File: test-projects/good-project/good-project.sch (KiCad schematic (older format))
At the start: 3 parts, among them J1 Conn_01x02

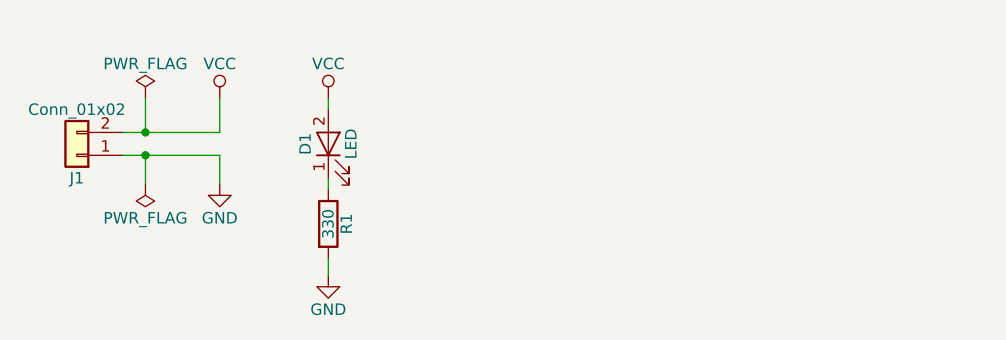
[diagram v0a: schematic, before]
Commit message: Handle schematic being created by newer versions of eeschema
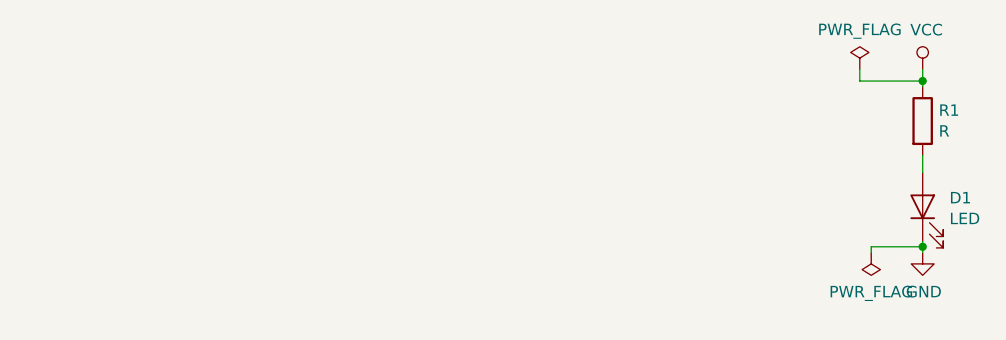
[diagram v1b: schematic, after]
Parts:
- removed D1: LED, LED_SMD:LED_0805_2012Metric, symbol LED
- removed J1: Conn_01x02, Connector_PinHeader_2.54mm:PinHeader_1x02_P2.54mm_Vertical, symbol Conn_01x02
- removed R1: 330, Resistor_SMD:R_0603_1608Metric, symbol R
- added D1: LED, symbol Device:LED
- added R1: R, symbol Device:R
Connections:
- net GND: now also D1.1 (K)
- net VCC: now also R1.1
- new net: D1.2 (A), R1.2
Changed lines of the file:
@@
-EESchema Schematic File Version 2
+EESchema Schematic File Version 4
 LIBS:good-project-cache
-EELAYER 25 0
+EELAYER 26 0
 EELAYER END
 $Descr A4 11693 8268
@@
 $EndDescr
 $Comp
-L R R1
-U 1 1 5CA32696
-P 3100 3425
-F 0 "R1" V 3180 3425 50  0000 C CNN
-F 1 "330" V 3100 3425 50  0000 C CNN
-F 2 "Resistor_SMD:R_0603_1608Metric" V 3030 3425 50  0001 C CNN
-F 3 "" H 3100 3425 50  0001 C CNN
-	1    3100 3425
+L Device:R R1
+U 1 1 5CA75BFC
+P 5700 2975
+F 0 "R1" H 5770 3021 50  0000 L CNN
+F 1 "R" H 5770 2930 50  0000 L CNN
+F 2 "" V 5630 2975 50  0001 C CNN
+F 3 "" H 5700 2975 50  0001 C CNN
+	1    5700 2975
 	1    0    0    -1
 $EndComp
 $Comp
-L LED D1
-U 1 1 5CA326B7
-P 3100 3075
-F 0 "D1" H 3100 3175 50  0000 C CNN
-F 1 "LED" H 3100 2975 50  0000 C CNN
-F 2 "LED_SMD:LED_0805_2012Metric" H 3100 3075 50  0001 C CNN
-F 3 "" H 3100 3075 50  0001 C CNN
-	1    3100 3075
+L Device:LED D1
+U 1 1 5CA75CA1
+P 5700 3350
+F 0 "D1" V 5738 3233 50  0000 R CNN
+F 1 "LED" V 5647 3233 50  0000 R CNN
+F 2 "" H 5700 3350 50  0001 C CNN
+F 3 "" H 5700 3350 50  0001 C CNN
+	1    5700 3350
 	0    -1   -1   0
 $EndComp
 $Comp
-L VCC #PWR01
-U 1 1 5CA32709
-P 3100 2875
-F 0 "#PWR01" H 3100 2725 50  0001 C CNN
-F 1 "VCC" H 3100 3025 50  0000 C CNN
-F 2 "" H 3100 2875 50  0001 C CNN
-F 3 "" H 3100 2875 50  0001 C CNN
-	1    3100 2875
+L power:VCC #PWR0101
+U 1 1 5CA75DE1
+P 5700 2750
+F 0 "#PWR0101" H 5700 2600 50  0001 C CNN
+F 1 "VCC" H 5717 2923 50  0000 C CNN
+F 2 "" H 5700 2750 50  0001 C CNN
+F 3 "" H 5700 2750 50  0001 C CNN
+	1    5700 2750
 	1    0    0    -1
 $EndComp
 $Comp
-L Conn_01x02 J1
-U 1 1 5CA32731
-P 2000 3125
-F 0 "J1" H 2000 3225 50  0000 C CNN
-F 1 "Conn_01x02" H 2000 2925 50  0000 C CNN
-F 2 "Connector_PinHeader_2.54mm:PinHeader_1x02_P2.54mm_Vertical" H 2000 3125 50  0001 C CNN
-F 3 "" H 2000 3125 50  0001 C CNN
-	1    2000 3125
-	-1   0    0    1
-$EndComp
-$Comp
-L VCC #PWR02
-U 1 1 5CA327B9
-P 2625 2875
-F 0 "#PWR02" H 2625 2725 50  0001 C CNN
-F 1 "VCC" H 2625 3025 50  0000 C CNN
-F 2 "" H 2625 2875 50  0001 C CNN
-F 3 "" H 2625 2875 50  0001 C CNN
-	1    2625 2875
+L power:GND #PWR0102
+U 1 1 5CA75E87
+P 5700 3550
+F 0 "#PWR0102" H 5700 3300 50  0001 C CNN
+F 1 "GND" H 5705 3377 50  0000 C CNN
+F 2 "" H 5700 3550 50  0001 C CNN
+F 3 "" H 5700 3550 50  0001 C CNN
+	1    5700 3550
 	1    0    0    -1
 $EndComp
 Wire Wire Line
-	2200 3025 2625 3025
+	5700 3500 5700 3525
 Wire Wire Line
-	3100 2875 3100 2925
+	5700 3200 5700 3125
 Wire Wire Line
-	3100 3225 3100 3275
+	5700 2825 5700 2800
 $Comp
-L GND #PWR03
-U 1 1 5CA32803
-P 2625 3250
-F 0 "#PWR03" H 2625 3000 50  0001 C CNN
-F 1 "GND" H 2625 3100 50  0000 C CNN
-F 2 "" H 2625 3250 50  0001 C CNN
-F 3 "" H 2625 3250 50  0001 C CNN
-	1    2625 3250
+L power:PWR_FLAG #FLG0101
+U 1 1 5CA762A4
+P 5425 2750
+F 0 "#FLG0101" H 5425 2825 50  0001 C CNN
+F 1 "PWR_FLAG" H 5425 2924 50  0000 C CNN
+F 2 "" H 5425 2750 50  0001 C CNN
+F 3 "" H 5425 2750 50  0001 C CNN
+	1    5425 2750
 	1    0    0    -1
 $EndComp
 Wire Wire Line
-	2200 3125 2625 3125
+	5425 2750 5425 2800
+Wire Wire Line
+	5425 2800 5700 2800
+Connection ~ 5700 2800
+Wire Wire Line
+	5700 2800 5700 2750
 $Comp
-L PWR_FLAG #FLG04
-U 1 1 5CA33697
-P 2300 2875
-F 0 "#FLG04" H 2300 2950 50  0001 C CNN
-F 1 "PWR_FLAG" H 2300 3025 50  0000 C CNN
-F 2 "" H 2300 2875 50  0001 C CNN
-F 3 "" H 2300 2875 50  0001 C CNN
-	1    2300 2875
-	1    0    0    -1
-$EndComp
-Wire Wire Line
-	2625 3025 2625 2875
-Wire Wire Line
-	2300 2875 2300 3025
-Connection ~ 2300 3025
-$Comp
-L PWR_FLAG #FLG05
-U 1 1 5CA341D3
-P 2300 3250
-F 0 "#FLG05" H 2300 3325 50  0001 C CNN
-F 1 "PWR_FLAG" H 2300 3400 50  0000 C CNN
-F 2 "" H 2300 3250 50  0001 C CNN
-F 3 "" H 2300 3250 50  0001 C CNN
-	1    2300 3250
+L power:PWR_FLAG #FLG0102
+U 1 1 5CA76394
+P 5475 3550
+F 0 "#FLG0102" H 5475 3625 50  0001 C CNN
+F 1 "PWR_FLAG" H 5475 3723 50  0000 C CNN
+F 2 "" H 5475 3550 50  0001 C CNN
+F 3 "" H 5475 3550 50  0001 C CNN
+	1    5475 3550
 	-1   0    0    1
 $EndComp
 Wire Wire Line
-	2625 3125 2625 3250
+	5475 3550 5475 3525
 Wire Wire Line
-	2300 3250 2300 3125
-Connection ~ 2300 3125
-$Comp
-L GND #PWR?
-U 1 1 5CA38687
-P 3100 3650
-F 0 "#PWR?" H 3100 3400 50  0001 C CNN
-F 1 "GND" H 3100 3500 50  0000 C CNN
-F 2 "" H 3100 3650 50  0001 C CNN
-F 3 "" H 3100 3650 50  0001 C CNN
-	1    3100 3650
-	1    0    0    -1
-$EndComp
+	5475 3525 5700 3525
+Connection ~ 5700 3525
 Wire Wire Line
-	3100 3575 3100 3650
+	5700 3525 5700 3550
 $EndSCHEMATC

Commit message: Update test projects to KiCad 5
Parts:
- D1: footprint (none) -> Diode_SMD:D_0805_2012Metric
- R1: footprint (none) -> Resistor_SMD:R_0603_1608Metric
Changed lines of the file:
@@
 F 0 "R1" H 5770 3021 50  0000 L CNN
 F 1 "R" H 5770 2930 50  0000 L CNN
-F 2 "" V 5630 2975 50  0001 C CNN
+F 2 "Resistor_SMD:R_0603_1608Metric" V 5630 2975 50  0001 C CNN
 F 3 "" H 5700 2975 50  0001 C CNN
 	1    5700 2975
@@
 F 0 "D1" V 5738 3233 50  0000 R CNN
 F 1 "LED" V 5647 3233 50  0000 R CNN
-F 2 "" H 5700 3350 50  0001 C CNN
+F 2 "Diode_SMD:D_0805_2012Metric" H 5700 3350 50  0001 C CNN
 F 3 "" H 5700 3350 50  0001 C CNN
 	1    5700 3350
